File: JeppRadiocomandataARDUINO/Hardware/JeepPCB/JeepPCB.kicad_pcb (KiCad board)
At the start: 2 copper layers, 43 x 48.2 mm, 21 parts, among them J1 Radio, U1 ATmega328P-A, Y1 Crystal

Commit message: Test di aggiunta testpad
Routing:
- net Earth: track 90.5 -> 78.8 mm
- net Net-(J1-Pad3): track 0.00 -> 7.05 mm
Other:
- board text added: "https://github.com/GiovanniRaseraF"
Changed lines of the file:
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@@
   )
   (gr_rect (start 40 39.6) (end 83.05 87.85) (layer "Edge.Cuts") (width 0.1) (fill none))
+  (gr_text "https://github.com/GiovanniRaseraF" (at 54.65 86.6) (layer "B.SilkS")
+    (effects (font (size 1 1) (thickness 0.15)) (justify mirror))
+  )
   (segment (start 55.85 58.75) (end 55.85 57.35) (width 1.5) (layer "F.Cu") (net 1))
   (segment (start 44.55 50.6) (end 44.5 50.65) (width 2) (layer "F.Cu") (net 1))
@@
   (segment (start 59.2 58.75) (end 69.85 58.75) (width 1.5) (layer "F.Cu") (net 2))
   (segment (start 71.775 60.675) (end 70.1 59) (width 2) (layer "F.Cu") (net 2))
-  (segment (start 63.35 77.6) (end 65.25 77.6) (width 0.3) (layer "F.Cu") (net 2))
-  (segment (start 56.75 78.4) (end 62.55 78.4) (width 0.3) (layer "F.Cu") (net 2))
-  (segment (start 63.5 79.2) (end 62.75 78.45) (width 0.3) (layer "F.Cu") (net 2))
   (segment (start 78.5 71.65) (end 78.5 75.45) (width 0.3) (layer "F.Cu") (net 2))
   (segment (start 78.25 75.3) (end 78.3 75.25) (width 0.3) (layer "F.Cu") (net 2))
@@
   (segment (start 77.725 71.45) (end 78.3 71.45) (width 0.3) (layer "F.Cu") (net 2))
   (segment (start 77.25 80.65) (end 77 80.4) (width 0.3) (layer "F.Cu") (net 2))
-  (segment (start 65.25 79.2) (end 63.5 79.2) (width 0.3) (layer "F.Cu") (net 2))
   (segment (start 69.685 58.585) (end 70.1 59) (width 2) (layer "F.Cu") (net 2))
   (segment (start 77 80.4) (end 76.4 80.4) (width 0.3) (layer "F.Cu") (net 2))
   (segment (start 70.1 59) (end 71.899022 59) (width 2) (layer "F.Cu") (net 2))
-  (segment (start 62.55 78.4) (end 63.35 77.6) (width 0.3) (layer "F.Cu") (net 2))
   (segment (start 67.25 72.6) (end 67.65 73) (width 0.5) (layer "F.Cu") (net 3))
   (segment (start 56.75 77.6) (end 57.95 77.6) (width 0.3) (layer "F.Cu") (net 3))
@@
   (segment (start 68.415 44.335) (end 69.7 43.05) (width 1.5) (layer "B.Cu") (net 7))
   (segment (start 69.7 43.05) (end 74.1 43.05) (width 1.5) (layer "B.Cu") (net 7))
+  (segment (start 65.25 80.8) (end 68.2 80.8) (width 0.25) (layer "F.Cu") (net 8))
+  (segment (start 68.2 80.8) (end 71.1 83.7) (width 0.25) (layer "F.Cu") (net 8))
   (segment (start 60.6 72) (end 60.6 71.8) (width 0.5) (layer "F.Cu") (net 9))
   (segment (start 60.6 71.2) (end 60.6 71.05) (width 0.5) (layer "F.Cu") (net 9))

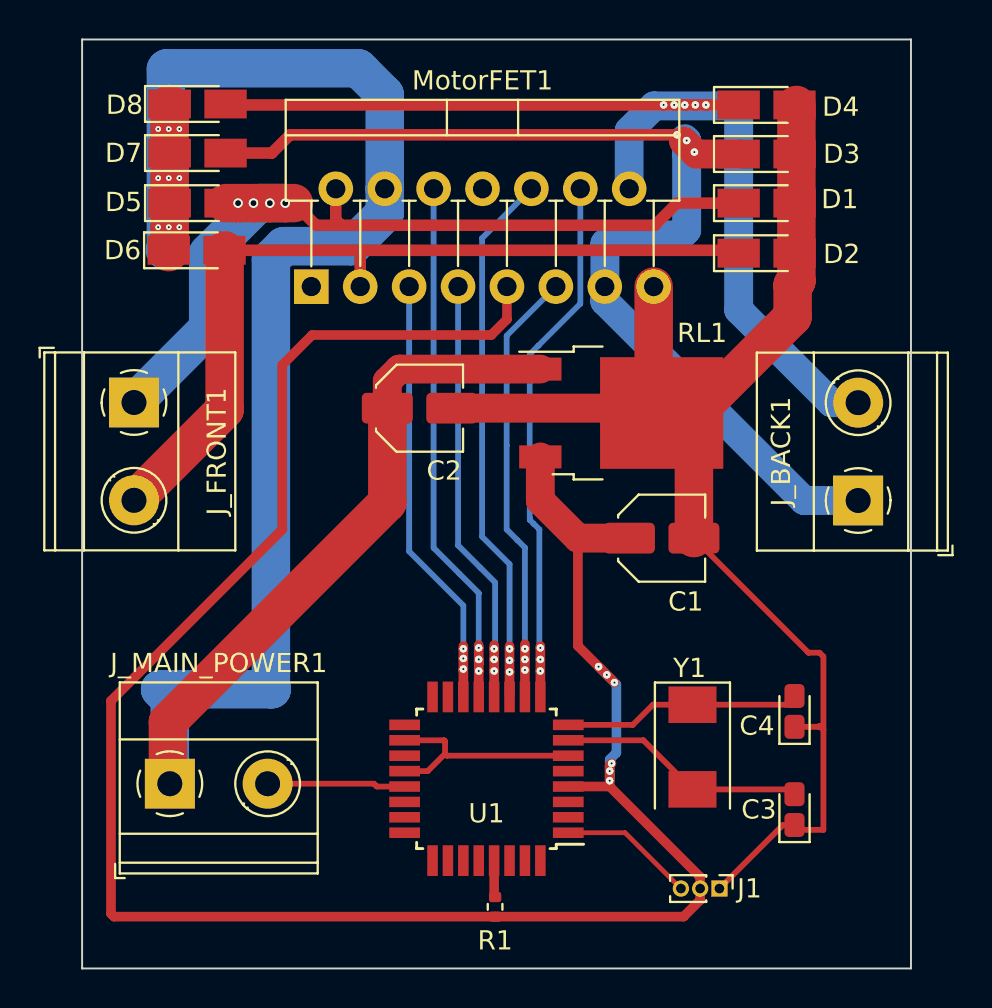
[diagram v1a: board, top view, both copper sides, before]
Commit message: Spostamento dei DIODI per dare più spazio alla saldatura
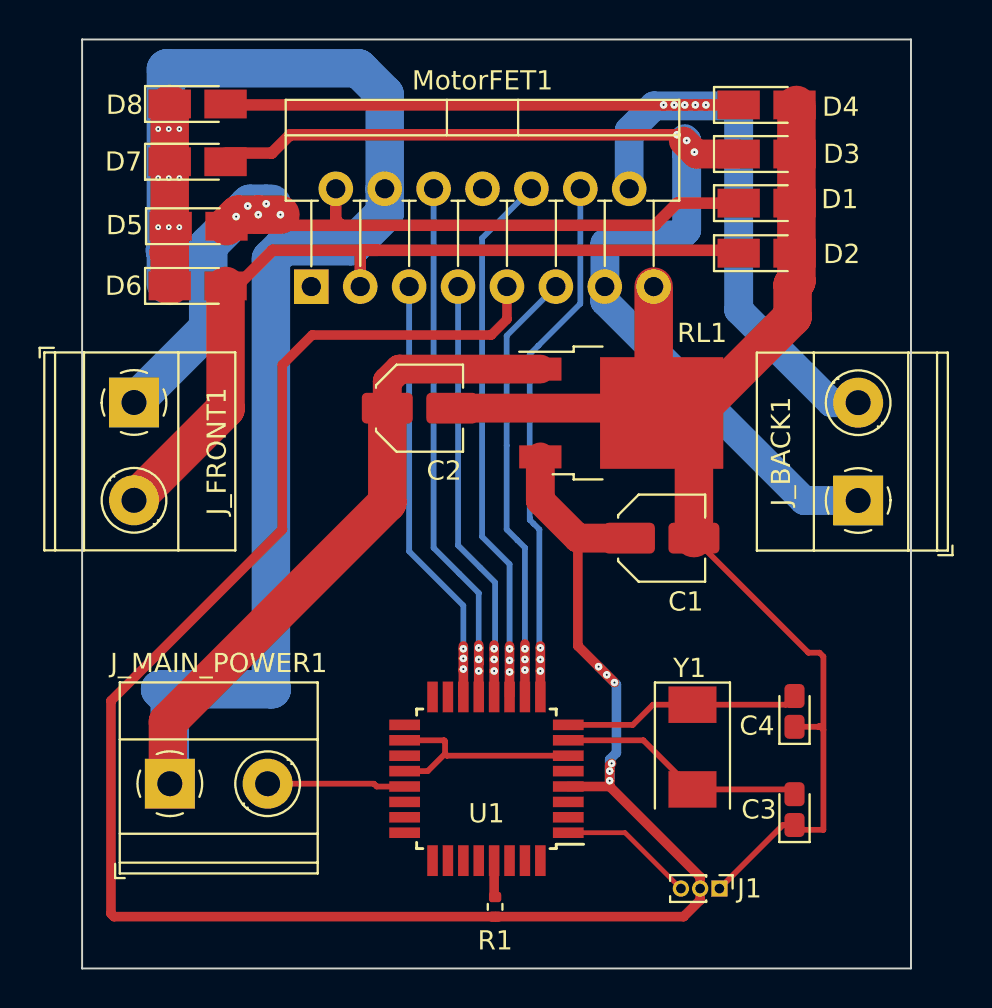
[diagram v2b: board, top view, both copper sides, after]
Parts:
- moved D6 1.85 mm to (46.0, 52.4)
- moved D5 1.20 mm to (46.0, 49.3)
- moved D7 0.45 mm to (46.0, 46.0)
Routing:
- net /5-12V: track 109.3 -> 112.8 mm
- net Net-(D1-Pad1): track 44.2 -> 43.6 mm, vias 4 -> 5
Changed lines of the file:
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@@
   )
   (footprint "Diode_SMD:D_MicroMELF_Handsoldering" (layer "F.Cu")
-    (at 45.95 50.55)
+    (at 46 52.4)
     (descr "Diode, MicroMELF, Hand Soldering, http://www.vishay.com/docs/85597/bzm55.pdf")
     (tags "MicroMELF Diode")
@@
   )
   (footprint "Diode_SMD:D_MicroMELF_Handsoldering" (layer "F.Cu")
-    (at 46 48.1)
+    (at 46.05 49.3)
     (descr "Diode, MicroMELF, Hand Soldering, http://www.vishay.com/docs/85597/bzm55.pdf")
     (tags "MicroMELF Diode")
@@
   )
   (footprint "Diode_SMD:D_MicroMELF_Handsoldering" (layer "F.Cu")
-    (at 46 45.5)
+    (at 46 45.95)
     (descr "Diode, MicroMELF, Hand Soldering, http://www.vishay.com/docs/85597/bzm55.pdf")
     (tags "MicroMELF Diode")
@@
   (segment (start 55.85 58.75) (end 55.85 57.35) (width 1.5) (layer "F.Cu") (net 1))
   (segment (start 44.55 50.6) (end 44.5 50.65) (width 2) (layer "F.Cu") (net 1))
+  (segment (start 44.55 50.7) (end 44.55 52.4) (width 2) (layer "F.Cu") (net 1))
   (segment (start 55.85 63.65) (end 55.85 58.75) (width 2) (layer "F.Cu") (net 1))
   (segment (start 55.85 57.35) (end 56.48 56.72) (width 1.5) (layer "F.Cu") (net 1))
   (segment (start 56.48 56.72) (end 63.8 56.72) (width 1.5) (layer "F.Cu") (net 1))
   (segment (start 44.455 78.155) (end 44.555 78.255) (width 2) (layer "F.Cu") (net 1))
+  (segment (start 44.5 50.65) (end 44.55 50.7) (width 2) (layer "F.Cu") (net 1))
   (segment (start 44.55 42.95) (end 44.55 50.6) (width 2) (layer "F.Cu") (net 1))
   (segment (start 44.455 75.045) (end 55.85 63.65) (width 2) (layer "F.Cu") (net 1))
@@
   (segment (start 49.85 73.35) (end 44.05 73.35) (width 2) (layer "B.Cu") (net 1))
   (segment (start 44.35 49.65) (end 44.35 50.5) (width 2) (layer "B.Cu") (net 1))
+  (segment (start 44.3 50.55) (end 44.35 50.6) (width 2) (layer "B.Cu") (net 1))
+  (segment (start 44.35 50.6) (end 44.35 52.3) (width 2) (layer "B.Cu") (net 1))
   (segment (start 44.05 73.35) (end 44.555 73.855) (width 2) (layer "B.Cu") (net 1))
   (segment (start 55.715 47.355) (end 55.715 48.627792) (width 2) (layer "B.Cu") (net 1))
@@
   (segment (start 67.75 76.65) (end 67.40104 76.99896) (width 0.5) (layer "B.Cu") (net 3))
   (segment (start 67.40104 76.99896) (end 67.40104 78.09896) (width 0.5) (layer "B.Cu") (net 3))
+  (segment (start 48 48.8) (end 48.1 48.7) (width 2) (layer "F.Cu") (net 4))
   (segment (start 53.175 48.975) (end 53.45 49.25) (width 0.6) (layer "F.Cu") (net 4))
-  (segment (start 50.55 48.1) (end 51 48.1) (width 2) (layer "F.Cu") (net 4))
+  (segment (start 50.85 49.25) (end 50.3 48.7) (width 0.6) (layer "F.Cu") (net 4))
   (segment (start 53.175 47.355) (end 53.175 48.975) (width 0.6) (layer "F.Cu") (net 4))
+  (segment (start 49.15 48.7) (end 50.3 48.7) (width 2) (layer "F.Cu") (net 4))
+  (segment (start 47.5 49.3) (end 47.9 48.9) (width 2) (layer "F.Cu") (net 4))
   (segment (start 53.08 47.45) (end 53.175 47.355) (width 1) (layer "F.Cu") (net 4))
   (segment (start 70.9 48.1) (end 69.75 49.25) (width 0.6) (layer "F.Cu") (net 4))
-  (segment (start 48.1 48.1) (end 48.9 48.1) (width 2) (layer "F.Cu") (net 4))
-  (segment (start 53.45 49.25) (end 52.15 49.25) (width 0.6) (layer "F.Cu") (net 4))
-  (segment (start 47.45 48.1) (end 48.1 48.1) (width 2) (layer "F.Cu") (net 4))
-  (segment (start 49.75 48.1) (end 50.55 48.1) (width 2) (layer "F.Cu") (net 4))
-  (segment (start 48.9 48.1) (end 49.75 48.1) (width 2) (layer "F.Cu") (net 4))
+  (segment (start 48.1 48.7) (end 49.15 48.7) (width 2) (layer "F.Cu") (net 4))
+  (segment (start 47.9 48.9) (end 48 48.8) (width 2) (layer "F.Cu") (net 4))
+  (segment (start 53.45 49.25) (end 50.85 49.25) (width 0.6) (layer "F.Cu") (net 4))
   (segment (start 74.1 48.1) (end 70.9 48.1) (width 0.6) (layer "F.Cu") (net 4))
-  (segment (start 52.15 49.25) (end 51 48.1) (width 0.6) (layer "F.Cu") (net 4))
   (segment (start 69.75 49.25) (end 53.45 49.25) (width 0.6) (layer "F.Cu") (net 4))
-  (via (at 50.55 48.1) (size 0.5) (drill 0.3) (layers "F.Cu" "B.Cu") (net 4))
-  (via (at 48.9 48.1) (size 0.5) (drill 0.3) (layers "F.Cu" "B.Cu") (net 4))
-  (via (at 48.1 48.1) (size 0.5) (drill 0.3) (layers "F.Cu" "B.Cu") (net 4))
-  (via (at 49.75 48.1) (size 0.5) (drill 0.3) (layers "F.Cu" "B.Cu") (net 4))
+  (via (at 49.564031 48.135969) (size 0.4) (drill 0.1) (layers "F.Cu" "B.Cu") (net 4))
+  (via (at 48 48.8) (size 0.4) (drill 0.1) (layers "F.Cu" "B.Cu") (net 4))
+  (via (at 50.3 48.7) (size 0.4) (drill 0.1) (layers "F.Cu" "B.Cu") (net 4))
+  (via (at 48.6 48.25) (size 0.4) (drill 0.1) (layers "F.Cu" "B.Cu") (net 4))
+  (via (at 49.15 48.7) (size 0.4) (drill 0.1) (layers "F.Cu" "B.Cu") (net 4))
+  (segment (start 46.54952 50.30048) (end 48.3 48.55) (width 2) (layer "B.Cu") (net 4))
+  (segment (start 48.6 48.25) (end 48.625 48.225) (width 2) (layer "B.Cu") (net 4))
   (segment (start 46.54952 54.60048) (end 42.695 58.455) (width 2) (layer "B.Cu") (net 4))
-  (segment (start 46.54952 50.70048) (end 46.54952 54.60048) (width 2) (layer "B.Cu") (net 4))
-  (segment (start 49.15 48.1) (end 46.54952 50.70048) (width 2) (layer "B.Cu") (net 4))
-  (segment (start 50.55 48.1) (end 49.15 48.1) (width 2) (layer "B.Cu") (net 4))
+  (segment (start 48.3 48.55) (end 48.6 48.25) (width 2) (layer "B.Cu") (net 4))
+  (segment (start 48.714031 48.135969) (end 49.564031 48.135969) (width 2) (layer "B.Cu") (net 4))
+  (segment (start 49.564031 48.135969) (end 49.85 48.135969) (width 2) (layer "B.Cu") (net 4))
+  (segment (start 46.54952 54.60048) (end 46.54952 50.30048) (width 2) (layer "B.Cu") (net 4))
+  (segment (start 48.625 48.225) (end 48.714031 48.135969) (width 2) (layer "B.Cu") (net 4))
+  (segment (start 49.9 50.55) (end 55.35 50.55) (width 0.6) (layer "F.Cu") (net 5))
+  (segment (start 48.05 52.4) (end 49.9 50.55) (width 0.6) (layer "F.Cu") (net 5))
   (segment (start 54.445 52.435) (end 54.445 50.605) (width 0.6) (layer "F.Cu") (net 5))
-  (segment (start 47.4 50.55) (end 54.5 50.55) (width 0.6) (layer "F.Cu") (net 5))
-  (segment (start 47.4 50.55) (end 47.4 58.83) (width 2) (layer "F.Cu") (net 5))
+  (segment (start 47.45 58.78) (end 47.45 52.4) (width 2) (layer "F.Cu") (net 5))
+  (segment (start 55.35 50.55) (end 73.95 50.55) (width 0.6) (layer "F.Cu") (net 5))
+  (segment (start 42.695 63.535) (end 47.45 58.78) (width 2) (layer "F.Cu") (net 5))
   (segment (start 54.445 50.605) (end 54.5 50.55) (width 0.6) (layer "F.Cu") (net 5))
-  (segment (start 47.4 58.83) (end 42.695 63.535) (width 2) (layer "F.Cu") (net 5))
   (segment (start 73.95 50.55) (end 74.1 50.7) (width 0.6) (layer "F.Cu") (net 5))
-  (segment (start 54.5 50.55) (end 73.95 50.55) (width 0.6) (layer "F.Cu") (net 5))
+  (segment (start 47.45 52.4) (end 48.05 52.4) (width 0.6) (layer "F.Cu") (net 5))
+  (segment (start 54.5 50.55) (end 55.35 50.55) (width 0.6) (layer "F.Cu") (net 5))
   (segment (start 70.9 44.55) (end 71.225 44.875) (width 0.6) (layer "F.Cu") (net 6))
   (segment (start 71.9 45.55) (end 71.8 45.45) (width 1.5) (layer "F.Cu") (net 6))

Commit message: Aggiornamento delle tracce
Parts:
- moved D2 1.65 mm to (75.6, 52.4)
- moved D1 1.35 mm to (75.5, 49.5)
- moved D3 0.50 mm to (75.5, 46.0)
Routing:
- net Net-(D2-Pad1): track 43.3 -> 44.1 mm
- net /5-12V: vias 9 -> 12
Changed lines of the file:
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@@
   )
   (footprint "Diode_SMD:D_MicroMELF_Handsoldering" (layer "F.Cu")
-    (at 75.55 48.1)
+    (at 75.55 49.45)
     (descr "Diode, MicroMELF, Hand Soldering, http://www.vishay.com/docs/85597/bzm55.pdf")
     (tags "MicroMELF Diode")
@@
   )
   (footprint "Diode_SMD:D_MicroMELF_Handsoldering" (layer "F.Cu")
-    (at 75.55 50.7)
+    (at 75.6 52.35)
     (descr "Diode, MicroMELF, Hand Soldering, http://www.vishay.com/docs/85597/bzm55.pdf")
     (tags "MicroMELF Diode")
@@
   )
   (footprint "Diode_SMD:D_MicroMELF_Handsoldering" (layer "F.Cu")
-    (at 75.55 45.55)
+    (at 75.5 46.05)
     (descr "Diode, MicroMELF, Hand Soldering, http://www.vishay.com/docs/85597/bzm55.pdf")
     (tags "MicroMELF Diode")
@@
     )
   )
+  (gr_line (start 43.2 53.7) (end 78.3 53.65) (layer "F.SilkS") (width 0.15))
   (gr_rect (start 40 39.6) (end 83.05 87.85) (layer "Edge.Cuts") (width 0.1) (fill none))
   (gr_text "https://github.com/GiovanniRaseraF" (at 54.65 86.6) (layer "B.SilkS")
@@
   (via (at 43.95 49.35) (size 0.3) (drill 0.1) (layers "F.Cu" "B.Cu") (net 1))
   (via (at 45.05 46.8) (size 0.3) (drill 0.1) (layers "F.Cu" "B.Cu") (net 1))
+  (via (at 45.1 50.85) (size 0.3) (drill 0.1) (layers "F.Cu" "B.Cu") (net 1))
   (via (at 44.5 49.35) (size 0.3) (drill 0.1) (layers "F.Cu" "B.Cu") (net 1))
   (via (at 43.95 46.8) (size 0.3) (drill 0.1) (layers "F.Cu" "B.Cu") (net 1))
+  (via (at 44.5 50.85) (size 0.3) (drill 0.1) (layers "F.Cu" "B.Cu") (net 1))
+  (via (at 43.95 50.85) (size 0.3) (drill 0.1) (layers "F.Cu" "B.Cu") (net 1))
   (segment (start 55.715 47.355) (end 55.715 42.465) (width 2) (layer "B.Cu") (net 1))
   (segment (start 54.35 41.1) (end 44.4 41.1) (width 2) (layer "B.Cu") (net 1))
@@
   (segment (start 67.75 76.65) (end 67.40104 76.99896) (width 0.5) (layer "B.Cu") (net 3))
   (segment (start 67.40104 76.99896) (end 67.40104 78.09896) (width 0.5) (layer "B.Cu") (net 3))
+  (segment (start 71.1 49.25) (end 71.3 49.45) (width 0.6) (layer "F.Cu") (net 4))
   (segment (start 48 48.8) (end 48.1 48.7) (width 2) (layer "F.Cu") (net 4))
   (segment (start 53.175 48.975) (end 53.45 49.25) (width 0.6) (layer "F.Cu") (net 4))
   (segment (start 50.85 49.25) (end 50.3 48.7) (width 0.6) (layer "F.Cu") (net 4))
+  (segment (start 53.45 49.25) (end 71.1 49.25) (width 0.6) (layer "F.Cu") (net 4))
   (segment (start 53.175 47.355) (end 53.175 48.975) (width 0.6) (layer "F.Cu") (net 4))
   (segment (start 49.15 48.7) (end 50.3 48.7) (width 2) (layer "F.Cu") (net 4))
   (segment (start 47.5 49.3) (end 47.9 48.9) (width 2) (layer "F.Cu") (net 4))
   (segment (start 53.08 47.45) (end 53.175 47.355) (width 1) (layer "F.Cu") (net 4))
-  (segment (start 70.9 48.1) (end 69.75 49.25) (width 0.6) (layer "F.Cu") (net 4))
+  (segment (start 71.3 49.45) (end 74.1 49.45) (width 0.6) (layer "F.Cu") (net 4))
   (segment (start 48.1 48.7) (end 49.15 48.7) (width 2) (layer "F.Cu") (net 4))
   (segment (start 47.9 48.9) (end 48 48.8) (width 2) (layer "F.Cu") (net 4))
   (segment (start 53.45 49.25) (end 50.85 49.25) (width 0.6) (layer "F.Cu") (net 4))
-  (segment (start 74.1 48.1) (end 70.9 48.1) (width 0.6) (layer "F.Cu") (net 4))
-  (segment (start 69.75 49.25) (end 53.45 49.25) (width 0.6) (layer "F.Cu") (net 4))
   (via (at 49.564031 48.135969) (size 0.4) (drill 0.1) (layers "F.Cu" "B.Cu") (net 4))
   (via (at 48 48.8) (size 0.4) (drill 0.1) (layers "F.Cu" "B.Cu") (net 4))
@@
   (segment (start 48.625 48.225) (end 48.714031 48.135969) (width 2) (layer "B.Cu") (net 4))
   (segment (start 49.9 50.55) (end 55.35 50.55) (width 0.6) (layer "F.Cu") (net 5))
+  (segment (start 74.15 52.35) (end 72.95 52.35) (width 0.6) (layer "F.Cu") (net 5))
   (segment (start 48.05 52.4) (end 49.9 50.55) (width 0.6) (layer "F.Cu") (net 5))
   (segment (start 54.445 52.435) (end 54.445 50.605) (width 0.6) (layer "F.Cu") (net 5))
+  (segment (start 55.35 50.55) (end 71.15 50.55) (width 0.6) (layer "F.Cu") (net 5))
   (segment (start 47.45 58.78) (end 47.45 52.4) (width 2) (layer "F.Cu") (net 5))
-  (segment (start 55.35 50.55) (end 73.95 50.55) (width 0.6) (layer "F.Cu") (net 5))
   (segment (start 42.695 63.535) (end 47.45 58.78) (width 2) (layer "F.Cu") (net 5))
   (segment (start 54.445 50.605) (end 54.5 50.55) (width 0.6) (layer "F.Cu") (net 5))
-  (segment (start 73.95 50.55) (end 74.1 50.7) (width 0.6) (layer "F.Cu") (net 5))
   (segment (start 47.45 52.4) (end 48.05 52.4) (width 0.6) (layer "F.Cu") (net 5))
+  (segment (start 72.95 52.35) (end 71.15 50.55) (width 0.6) (layer "F.Cu") (net 5))
   (segment (start 54.5 50.55) (end 55.35 50.55) (width 0.6) (layer "F.Cu") (net 5))
   (segment (start 70.9 44.55) (end 71.225 44.875) (width 0.6) (layer "F.Cu") (net 6))
-  (segment (start 71.9 45.55) (end 71.8 45.45) (width 1.5) (layer "F.Cu") (net 6))
   (segment (start 71.8 45.45) (end 71.225 44.875) (width 1.5) (layer "F.Cu") (net 6))
   (segment (start 49.85 45.5) (end 50.8 44.55) (width 0.6) (layer "F.Cu") (net 6))
-  (segment (start 74.1 45.55) (end 71.9 45.55) (width 1.5) (layer "F.Cu") (net 6))
+  (segment (start 74.05 46.05) (end 72.4 46.05) (width 1.5) (layer "F.Cu") (net 6))
   (segment (start 50.8 44.55) (end 70.9 44.55) (width 0.6) (layer "F.Cu") (net 6))
   (segment (start 47.45 45.5) (end 49.85 45.5) (width 0.6) (layer "F.Cu") (net 6))
+  (segment (start 72.4 46.05) (end 71.8 45.45) (width 1.5) (layer "F.Cu") (net 6))
   (via (at 71.4 44.85) (size 0.4) (drill 0.1) (layers "F.Cu" "B.Cu") (net 6))
   (via (at 71.8 45.45) (size 0.4) (drill 0.1) (layers "F.Cu" "B.Cu") (net 6))
